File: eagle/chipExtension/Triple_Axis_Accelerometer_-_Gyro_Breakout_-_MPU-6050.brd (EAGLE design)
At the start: 17 parts, among them U1 MPU-6050-1, U3 PCA9685

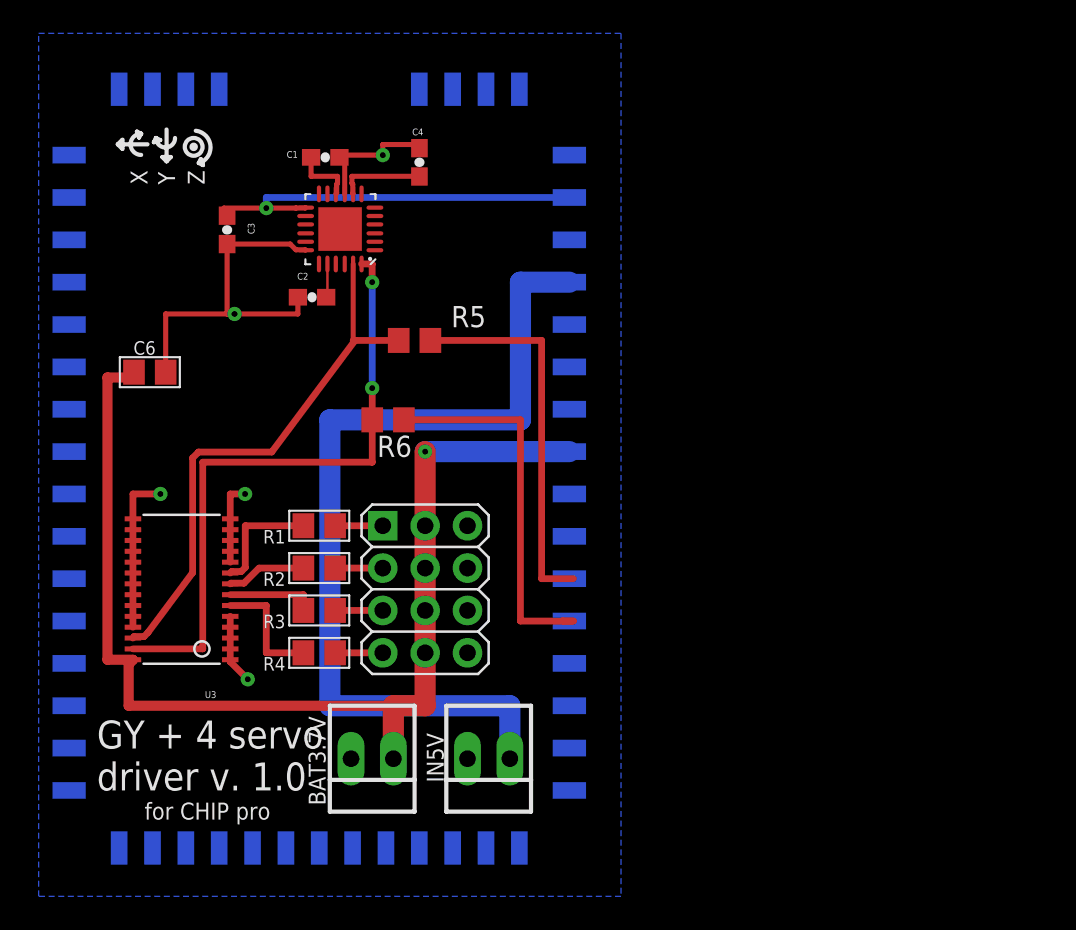
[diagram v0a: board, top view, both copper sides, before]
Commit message: Adding holes to the PCB on eagle and enhancing the freeca model of cylinder prototype 3.
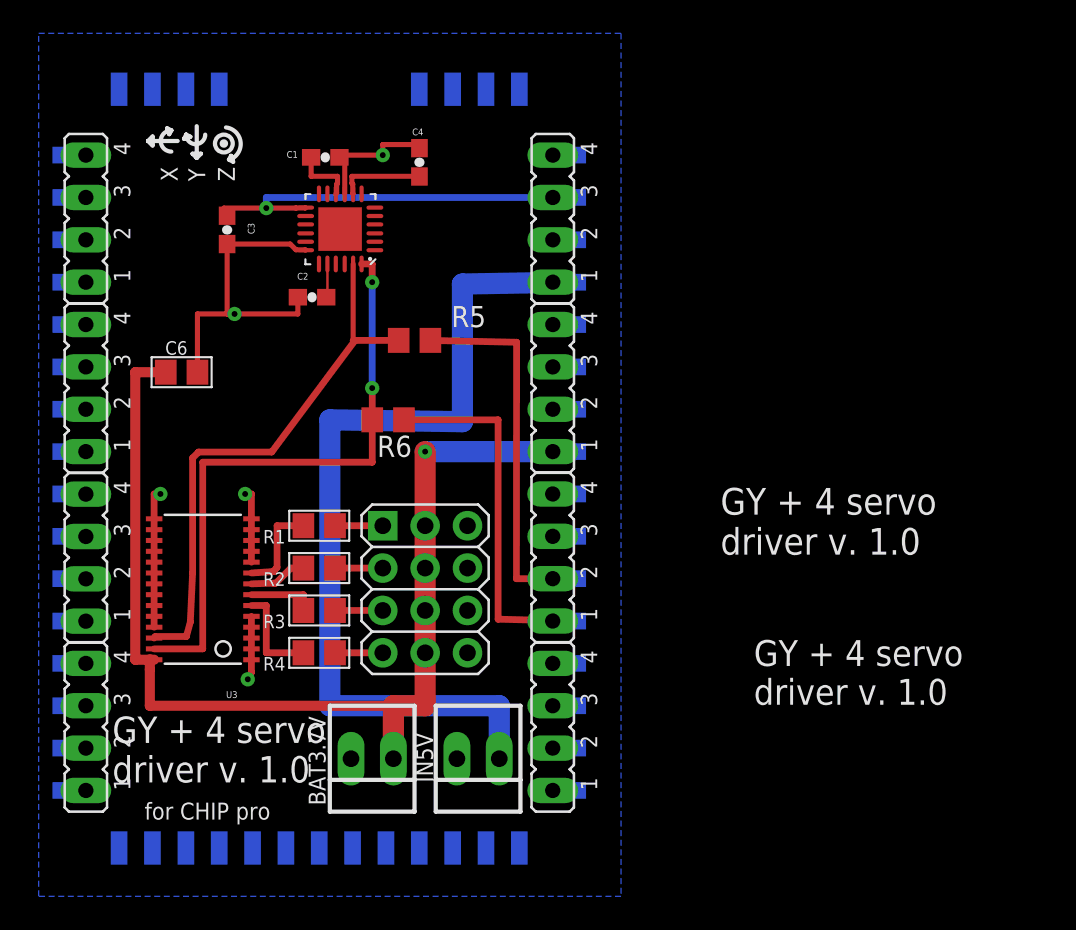
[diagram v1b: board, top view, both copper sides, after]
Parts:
- added JP2, JP3, JP4, JP5, JP6, JP7, JP8, JP9: (no value), jumper:JP4
- moved C6 1.90 mm to (19.7, 47.9)
- moved U3 1.27 mm to (21.0, 34.9)
- moved IN5V 0.63 mm to (37.5, 24.8)
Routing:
- net GND: track 49.0 -> 45.0 mm
- net SDA: track 60.9 -> 58.9 mm
- net PWM2: track 4.78 -> 3.49 mm
- net PWM1: track 5.33 -> 4.06 mm
- net PWM0: track 7.22 -> 5.95 mm
- net PWM3: track 7.03 -> 5.85 mm
- net VCC: track 68.1 -> 67.4 mm
- net N$9: track 53.7 -> 53.1 mm

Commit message: Adding jumper to eagle files and enhancing the freecad model of cylinderPrototype3.
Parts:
- added JP10: (no value), jumper:JP1
- moved BAT3.7V 12.8 mm to (18.3, 24.2)
- moved IN5V 12.7 mm to (24.8, 24.1)
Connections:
- net VCC: now also JP10.1, JP10.2
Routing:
- net N$9: track 53.1 -> 46.1 mm
- net VCC: track 67.4 -> 65.4 mm
- net GND: track 45.0 -> 45.7 mm
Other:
- board text added: "0"
- board text added: "1"
- board text added: "2"
- board text added: "3"

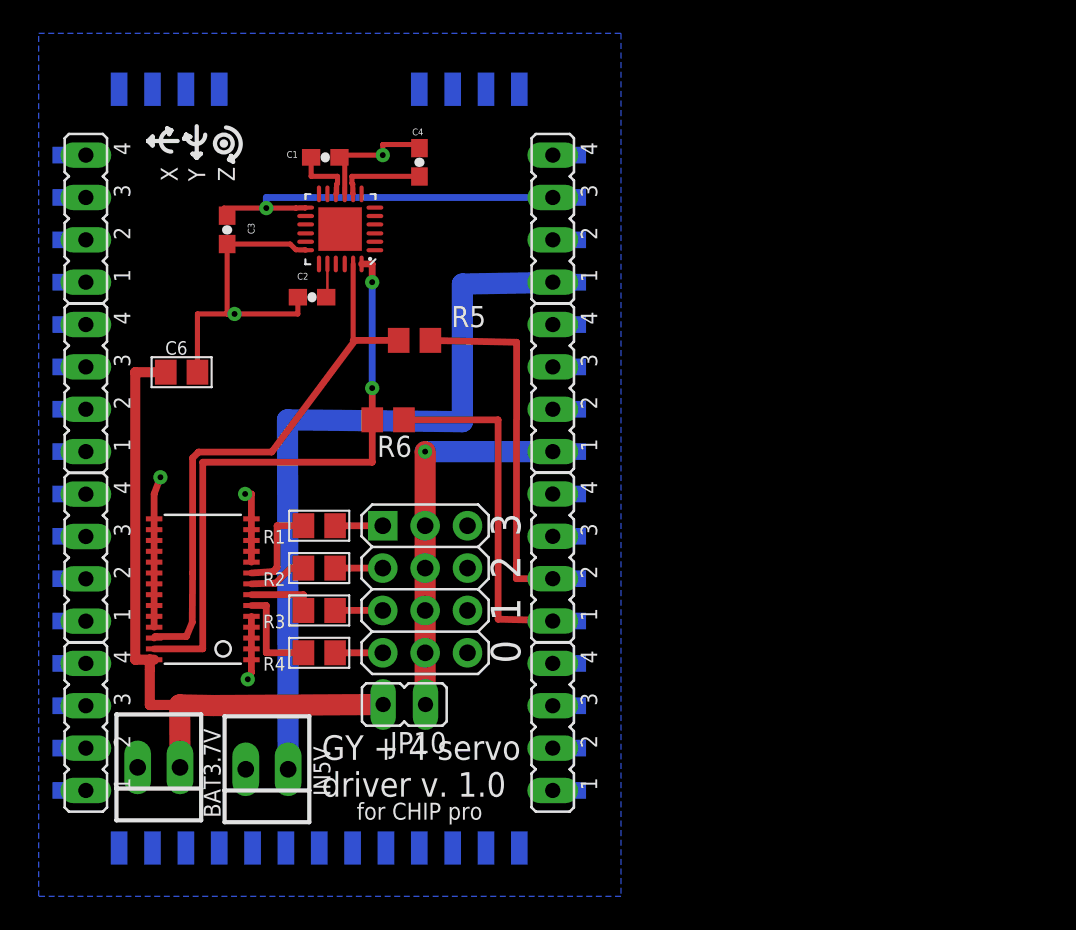
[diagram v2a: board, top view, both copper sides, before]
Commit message: improve eagle design
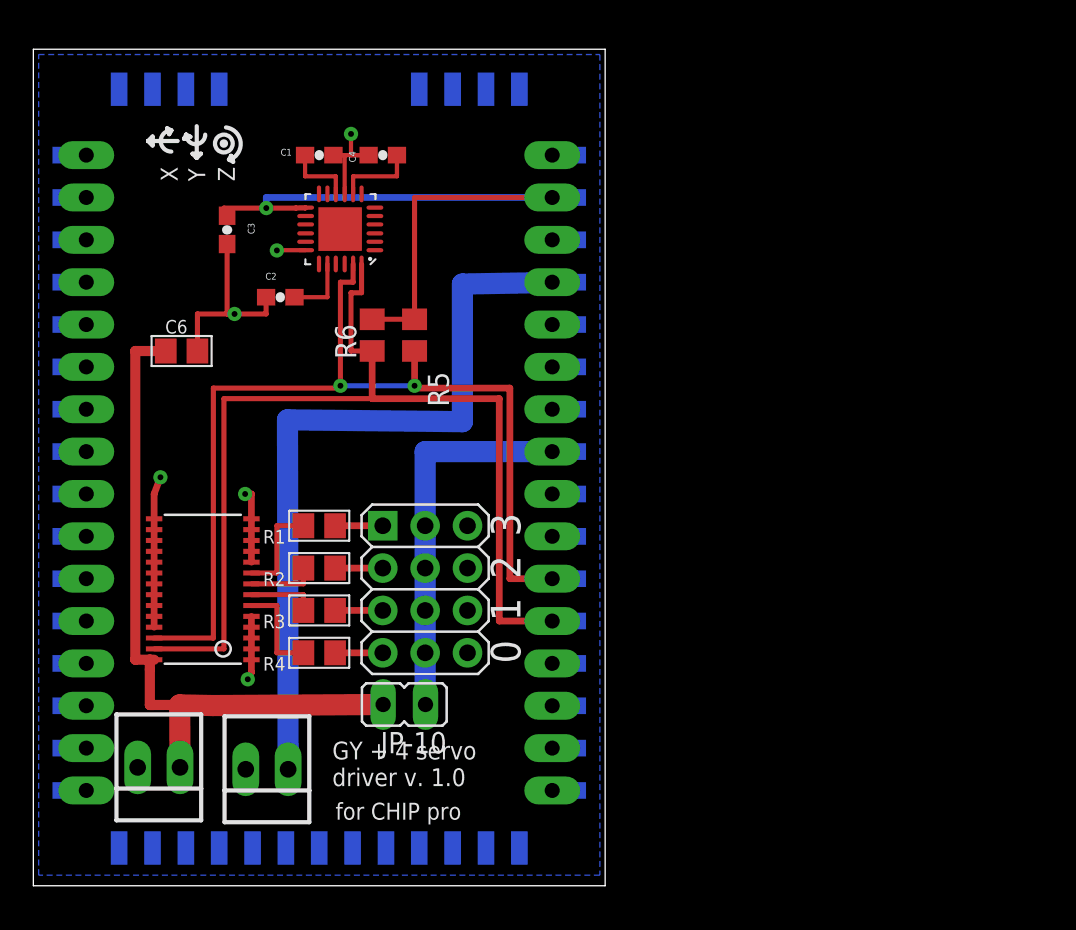
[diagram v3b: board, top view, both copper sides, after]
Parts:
- removed JP2, JP3, JP4, JP5, JP6, JP7, JP8, JP9: (no value), jumper:JP4
- JP-10: value (none) -> A
- U$1: value CHIP_PRO -> CHIP_PROHOLE; device CHIP_Pro-Footprint:CHIP_PRO -> CHIP_Pro-Footprint:CHIP_PRO_HOLE
- moved R6 5.17 mm to (31.1, 50.2), turned to 90 degrees
- moved C4 2.24 mm to (31.8, 61.0), turned to 180 degrees
- moved C2 1.90 mm to (25.6, 52.4)
- moved C6 1.27 mm to (19.7, 49.2)
- moved C1 0.39 mm to (27.9, 61.0)
- moved R5 0.32 mm to (33.7, 50.2), turned to 90 degrees
- renumbered JP10 to JP-10
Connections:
- net 3.3V: now also R5.2, R6.2, U$1.VCC3V3-1
- net GND: now also U$1.GND@0-1, U$1.GND@2-1, U$1.GND@3-1
- net IPSOUT: now also U$1.IPSOUT-1
- net N$9: now also U$1.CHG-IN-1
- net SCL: now also U$1.TWI1-SCK-1; no longer R5.2
- net SDA: now also U$1.TWI1-SDA-1; no longer R6.2
- net VCC: now also U$1.BAT-1
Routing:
- net 3.3V: track 24.4 -> 42.5 mm
- net GND: track 45.7 -> 38.5 mm, vias 5 -> 6
- net SCL: track 56.2 -> 60.7 mm, vias 0 -> 2
- net SDA: track 58.9 -> 62.2 mm, vias 2 -> 0
- net N$3: track 2.07 -> 3.97 mm
- net VCC: track 65.4 -> 66.7 mm, vias 1 -> 0
- net PWM2: track 3.49 -> 4.06 mm
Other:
- board outline added: 34.3 x 50.2 mm
